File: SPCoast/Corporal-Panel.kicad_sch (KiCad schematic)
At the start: 16 parts, among them U12031 0x2A, U12032 0x2B

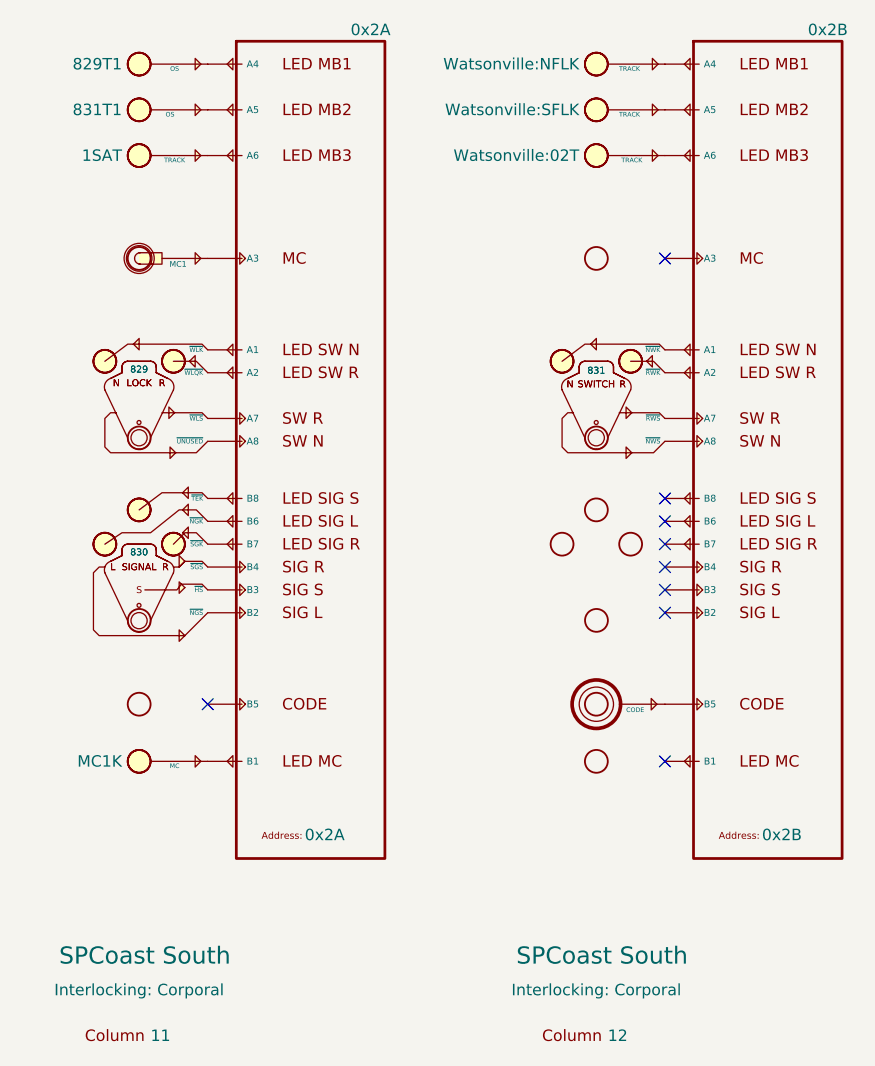
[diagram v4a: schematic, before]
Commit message: feat(kicad): deployment cases: Caltrain on a CMRInet node, Gilroy Interchange JMRI turnouts over MQTT
Gilroy Caltrain: field I/O drawn as per-bit CMRInet drivers (Driver-CMRI-IB/OB,
UA 30, 14 in / 20 out) with named devices for 3 switches, 5 track circuits and
7 heads (four encoder-wired, three lamp-wired). No processor is named: every
chip is on the hosted CMRInet bus, so the field unit runs on that bus's host.

Gilroy Interchange: proof of concept for JMRI turnouts and sensors over MQTT
(Driver-JMRI-Turnout, -Turnout-Feedback, -Sensor-Feedback) on switches 777
and 781. Known: the 777 drivers carry Address 771 (typo, fixed by the
follow-up rewrite); the JMRI symbols fail lint_symbol_fields (Pin.D names no
pin, Topic/States casing), also fixed by the rewrite.

Libraries: Railroad-HardwareIO gains Driver-CMRI-IB/OB and the four JMRI
drivers; Railroad-Field's Device-Head-CPL pins renumbered top down (G, Y, R).
Nine other sheets were re-saved by KiCad with property placements only.

Verified:
- kicad-cli ERC: 0 violations, whole project
- every Caltrain and Gilroy Interchange device binds; no duplicate CMRI bits
- netlist_diff vs post-sync.net: only additions on the two sheets (49 parts,
  34 nets, 68 nodes), nothing lost or changed elsewhere
- library-owned field drift on the new instances: 0

Co-Authored-By: Claude Fable 5.1 <noreply@anthropic.com>
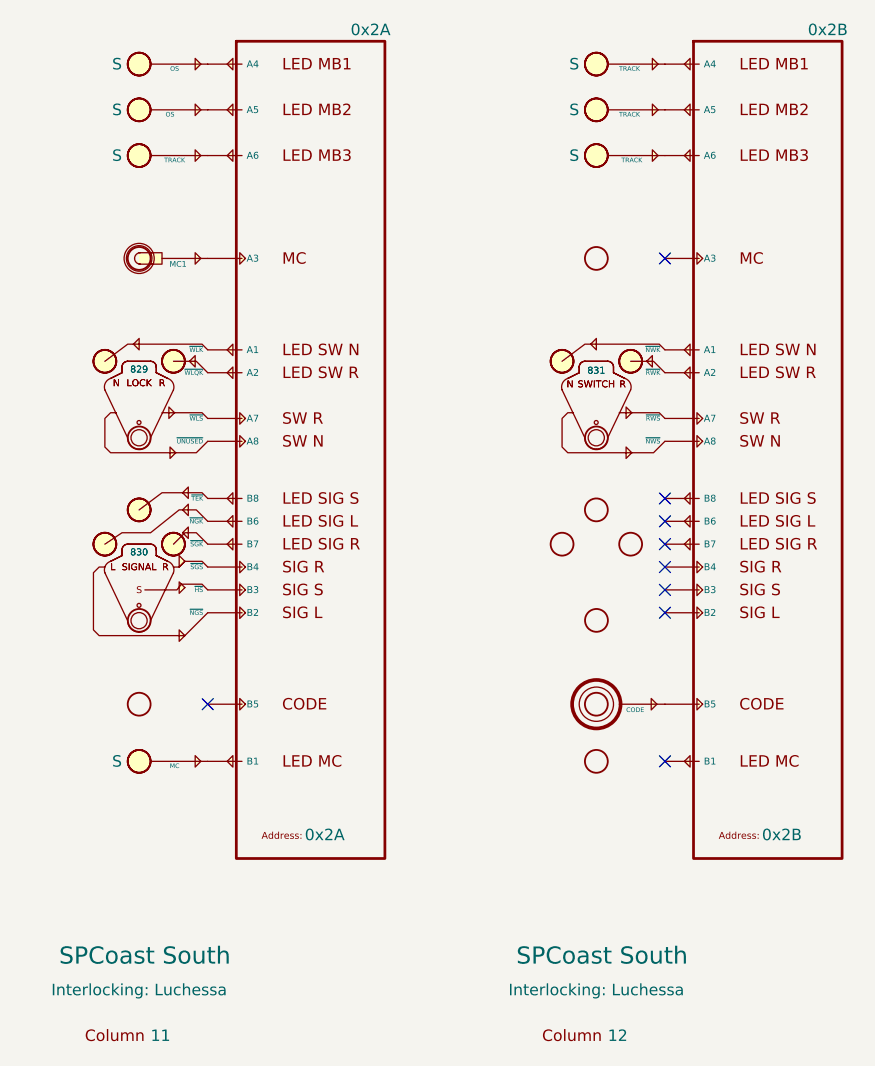
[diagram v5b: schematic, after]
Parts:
- COL12031, COL12032: Interlocking Corporal -> Luchessa
- LMP12111: IndicationToken 829T1 -> S
- LMP12112: IndicationToken 831T1 -> S
- LMP12113: IndicationToken 1SAT -> S
- LMP12121: IndicationToken Watsonville:NFLK -> S
- LMP12122: IndicationToken Watsonville:SFLK -> S
- LMP12123: IndicationToken Watsonville:02T -> S
- MCK12011: IndicationToken MC1K -> S
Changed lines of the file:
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@@
 			)
 		)
-		(property "IndicationToken" "829T1"
+		(property "IndicationToken" "S"
 			(at 78.105 26.67 0)
 			(show_name no)
@@
 			)
 		)
-		(property "IndicationToken" "Watsonville:02T"
+		(property "IndicationToken" "S"
 			(at 128.905 36.83 0)
 			(show_name no)
@@
 			)
 		)
-		(property "IndicationToken" "1SAT"
+		(property "IndicationToken" "S"
 			(at 78.105 36.83 0)
 			(show_name no)
@@
 			)
 		)
-		(property "IndicationToken" "MC1K"
+		(property "IndicationToken" "S"
 			(at 78.105 104.14 0)
 			(show_name no)
@@
 			)
 		)
-		(property "IndicationToken" "Watsonville:NFLK"
+		(property "IndicationToken" "S"
 			(at 128.905 26.67 0)
 			(show_name no)
@@
 			)
 		)
-		(property "ki_locked" ""
-			(at 130.81 63.5 0)
-			(hide yes)
-			(show_name no)
-			(do_not_autoplace no)
-			(effects
-				(font
-					(size 1.27 1.27)
-				)
-			)
-		)
 		(pin "1"
 		)
@@
 			)
 		)
-		(property "ki_locked" ""
-			(at 80.01 83.82 0)
-			(hide yes)
-			(show_name no)
-			(do_not_autoplace no)
-			(effects
-				(font
-					(size 1.27 1.27)
-				)
-			)
-		)
 		(pin "5"
 		)
@@
 			)
 		)
-		(property "IndicationToken" "Watsonville:SFLK"
+		(property "IndicationToken" "S"
 			(at 128.905 31.75 0)
 			(show_name no)
@@
 			)
 		)
-		(property "ki_locked" ""
-			(at 130.81 63.5 0)
-			(hide yes)
-			(show_name no)
-			(do_not_autoplace no)
-			(effects
-				(font
-					(size 1.27 1.27)
-				)
-			)
-		)
 		(pin "4"
 		)
@@
 			)
 		)
-		(property "IndicationToken" "831T1"
+		(property "IndicationToken" "S"
 			(at 78.105 31.75 0)
 			(show_name no)
@@
 			)
 		)
-		(property "Interlocking" "Corporal"
+		(property "Interlocking" "Luchessa"
 			(at 80.01 129.54 0)
 			(show_name yes)
@@
 			)
 		)
-		(property "Interlocking" "Corporal"
+		(property "Interlocking" "Luchessa"
 			(at 130.81 129.54 0)
 			(show_name yes)
@@
 			)
 		)
-		(property "ki_locked" ""
-			(at 80.01 63.5 0)
-			(hide yes)
-			(show_name no)
-			(do_not_autoplace no)
-			(effects
-				(font
-					(size 1.27 1.27)
-				)
-			)
-		)
 		(pin "4"
 		)
@@
 			)
 		)
-		(property "ki_locked" ""
-			(at 80.01 63.5 0)
-			(hide yes)
-			(show_name no)
-			(do_not_autoplace no)
-			(effects
-				(font
-					(size 1.27 1.27)
-				)
-			)
-		)
 		(pin "1"
 		)
@@
 			(hide yes)
 			(show_name no)
-			(do_not_autoplace no)
-			(effects
-				(font
-					(size 1.27 1.27)
-				)
-			)
-		)
-		(property "ki_locked" ""
-			(at 80.01 83.82 0)
-			(hide yes)
-			(show_name no)

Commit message: refactor(kicad): mast anchors with explicit indication-to-aspect casts; restore fields KiCad reset
Second pass after the cast chains (b4c58d3), decided 2026-10-17: the per-head
anchors Head-CPL/CL/Semaphore were the mast's indication table collapsed into
a symbol. The chain is now

    [Mast 774NAB] -indication- [Cast-Aspect-CPL unit B] -aspect- [Cast-Encoder-CPL] -bits- [chip]

Cast-Aspect-CPL/CL/Semaphore are multi-unit casts, one unit per head letter
(A..E), so placing unit B beside mast 774N is head 774NB with nothing typed;
the reader derives every head name from mast plus unit. Style's home is the
aspect cast. The project ERC now ignores missing_unit and missing_input_pin,
since an aspect cast places only the units its mast has.

CMRI bits: Address is the node (the chip every bit folds into, as for every
other driver), Bit is the bit, UA = ${Address} is a display echo, Value =
UA${Address}.IN.${Bit}.

Restore (SPCoast/edits/2026-10-17-restore-reset-fields.py): the owner's last
KiCad save before 857cae2 ran "update symbols from library" with field reset,
putting library defaults into per-instance fields on nine sheets: every
PanelLamp IndicationToken ("S"), PanelColumn Interlocking ("Luchessa"),
Luchessa encoding Station ("Panel"), Sargent Exp2 PCA9685-PWM 0x27 -> 0x20
(colliding with Exp3), and the 34 Caltrain bit numbers. All 98 values are
restored from the last good netlist export, embedded in the script.

Scripts: SPCoast/edits/2026-10-17-mast-chain.py (second pass; reuses the
first pass's helpers), 2026-10-17-restore-reset-fields.py. __pycache__/
added to .gitignore.

Verified:
- post-restore netlist vs the last good export: no field differs except on
  the anchors the first pass replaced and the intended JMRI blanks
- lint_symbol_fields: 93 symbols, 0 errors (per-unit cast rule)
- kicad-cli ERC: 0 violations; netlist export without warnings
- gate vs post-restore: nets not touching an anchor identical; all 11 aspect
  nets re-sourced from a Cast-Aspect un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
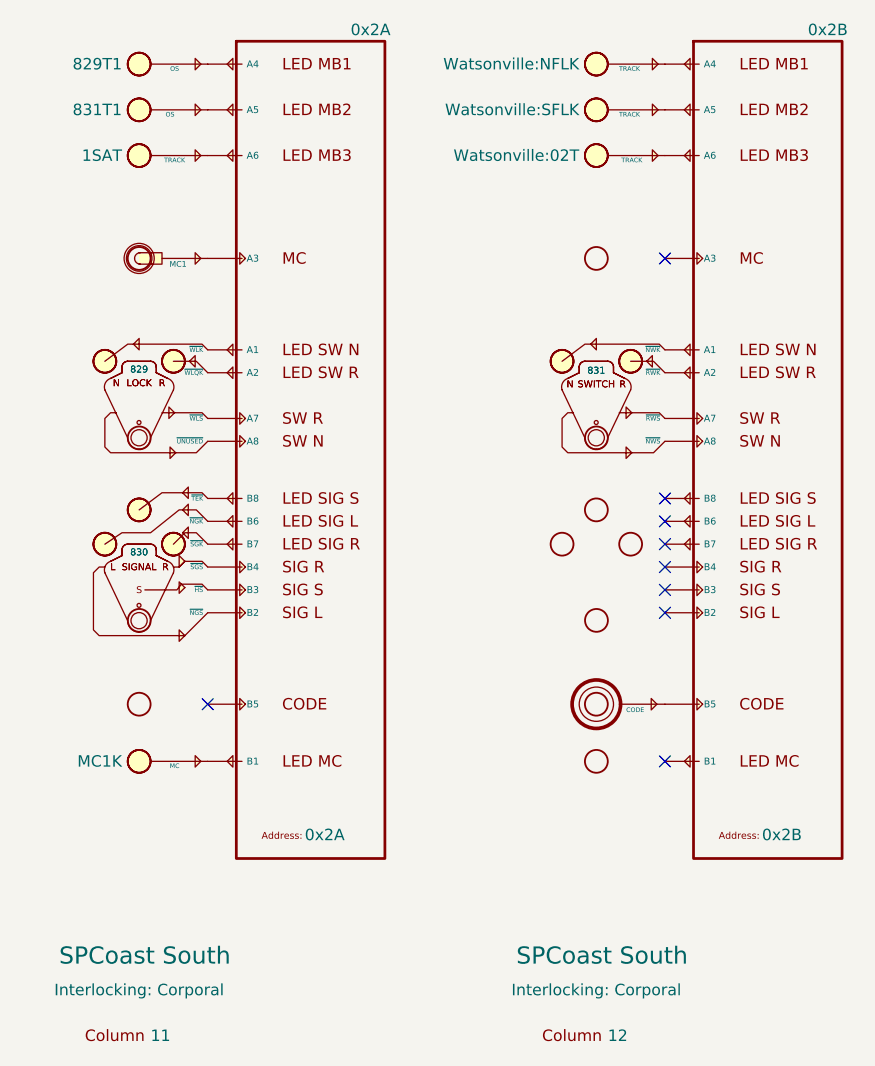
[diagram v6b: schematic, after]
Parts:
- COL12031, COL12032: Interlocking Luchessa -> Corporal
- LMP12111: IndicationToken S -> 829T1
- LMP12112: IndicationToken S -> 831T1
- LMP12113: IndicationToken S -> 1SAT
- LMP12121: IndicationToken S -> Watsonville:NFLK
- LMP12122: IndicationToken S -> Watsonville:SFLK
- LMP12123: IndicationToken S -> Watsonville:02T
- MCK12011: IndicationToken S -> MC1K
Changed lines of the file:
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@@
 			)
 		)
-		(property "IndicationToken" "S"
+		(property "IndicationToken" "829T1"
 			(at 78.105 26.67 0)
 			(show_name no)
@@
 			)
 		)
-		(property "IndicationToken" "S"
+		(property "IndicationToken" "Watsonville:02T"
 			(at 128.905 36.83 0)
 			(show_name no)
@@
 			)
 		)
-		(property "IndicationToken" "S"
+		(property "IndicationToken" "1SAT"
 			(at 78.105 36.83 0)
 			(show_name no)
@@
 			)
 		)
-		(property "IndicationToken" "S"
+		(property "IndicationToken" "MC1K"
 			(at 78.105 104.14 0)
 			(show_name no)
@@
 			)
 		)
-		(property "IndicationToken" "S"
+		(property "IndicationToken" "Watsonville:NFLK"
 			(at 128.905 26.67 0)
 			(show_name no)
@@
 			)
 		)
-		(property "IndicationToken" "S"
+		(property "IndicationToken" "Watsonville:SFLK"
 			(at 128.905 31.75 0)
 			(show_name no)
@@
 			)
 		)
-		(property "IndicationToken" "S"
+		(property "IndicationToken" "831T1"
 			(at 78.105 31.75 0)
 			(show_name no)
@@
 			)
 		)
-		(property "Interlocking" "Luchessa"
+		(property "Interlocking" "Corporal"
 			(at 80.01 129.54 0)
 			(show_name yes)
@@
 			)
 		)
-		(property "Interlocking" "Luchessa"
+		(property "Interlocking" "Corporal"
 			(at 130.81 129.54 0)
 			(show_name yes)

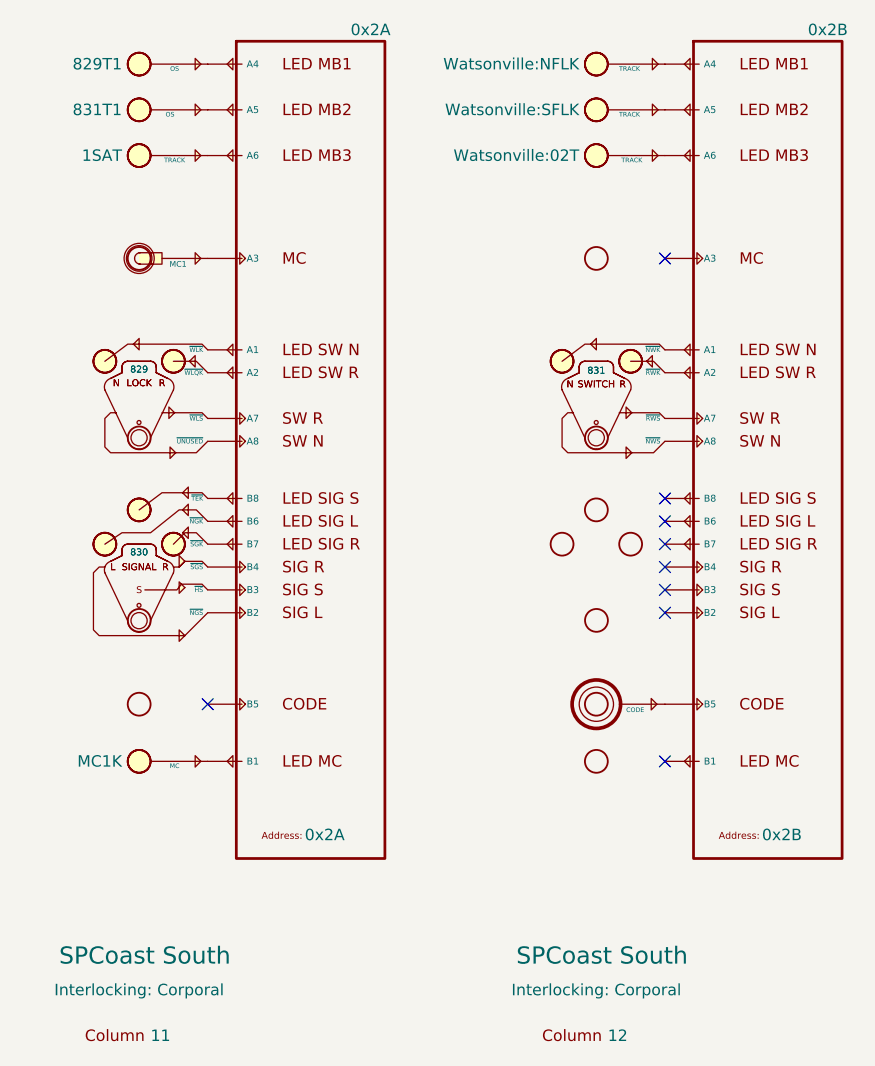
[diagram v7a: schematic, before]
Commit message: chore(kicad): owner edits: GPIO drivers carry Address, Sargent I2C addresses, CMRI body text from fields
Baseline of the owner's saved work before the ADR 0005 scripts:
- Driver-GPIO-Digital and Driver-GPIO-Pixel gain an Address field (the
  board pin); Value renders ${Address}; body text and arrow adjusted.
- Driver-CMRI-IB/OB body text renders UA${Address}.IN/OUT.${Bit} from
  the fields instead of ${VALUE}.
- Sargent, Gilroy Interchange and Luchessa GPIO instances carry Address;
  Sargent Exp2 back at 0x26, Exp3 0x27.
- All sheets resaved by KiCad 10 (reordering), project file
  used_designators cleared by KiCad.

Verified: no lock files; committed as saved, unverified by netlist (the
baseline netlist is exported in the next step).

Co-Authored-By: Claude Fable 5.1 <noreply@anthropic.com>
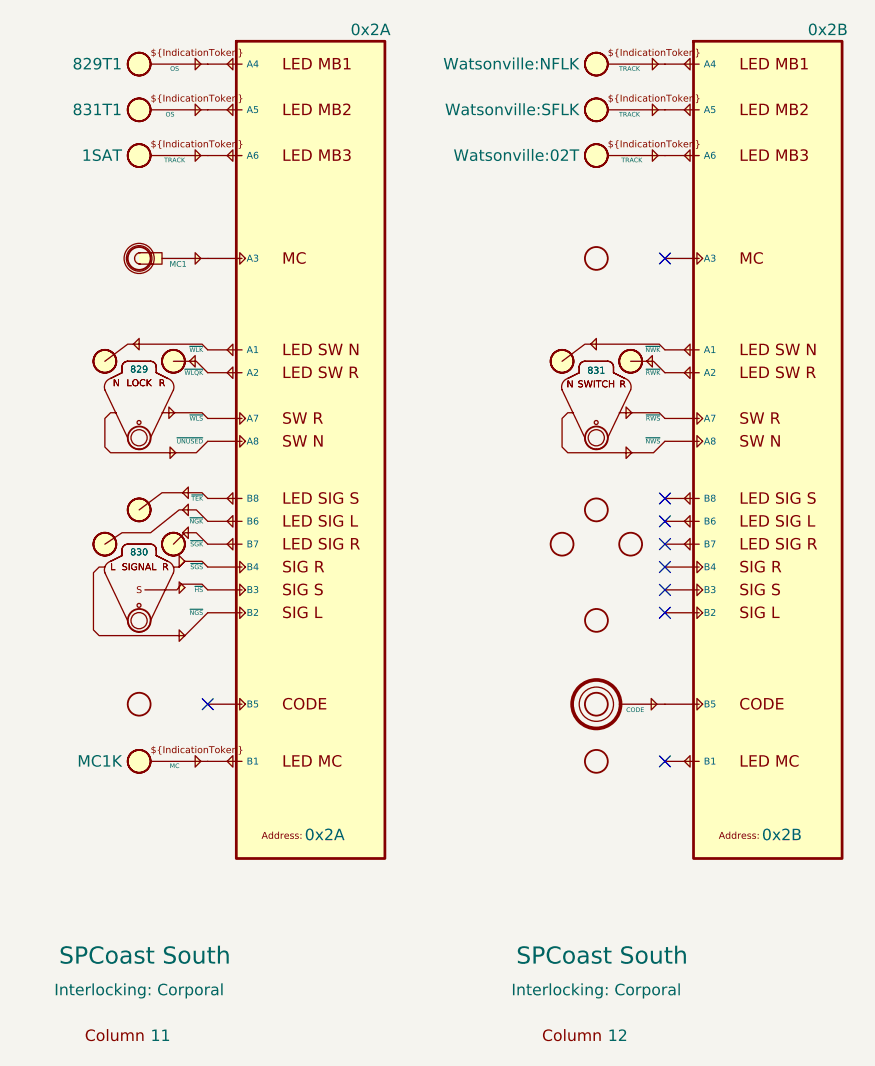
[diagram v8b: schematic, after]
